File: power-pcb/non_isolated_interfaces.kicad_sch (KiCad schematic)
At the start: 66 parts, among them J1 Network Connector, J2 Screw_Terminal_01x02, J3 STDC14, J4 USB_C_Receptacle_USB2.0_16P, U1 TPS5430DDA, U2 ECMF02-2AMX6, U3 AMS1117-3.3, U4 SN65HVD230

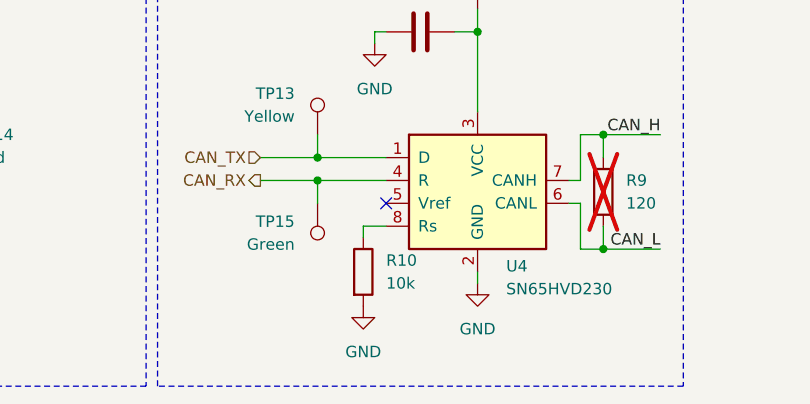
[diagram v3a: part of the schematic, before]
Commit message: power-pcb: change some 10k to 12k
JLCPCB doesn't offer a small package for the 10k resistors so some had
to be changed.
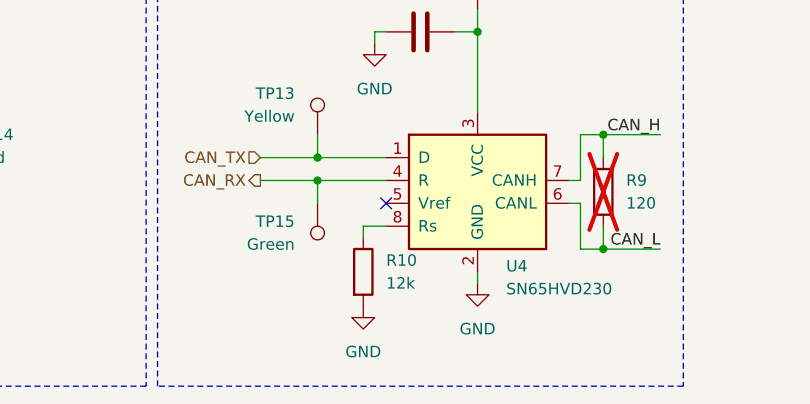
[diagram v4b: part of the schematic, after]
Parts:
- R1, R2: footprint Resistor_SMD:R_0603_1608Metric_Pad0.98x0.95mm_HandSolder -> Resistor_SMD:R_0805_2012Metric_Pad1.20x1.40mm_HandSolder; JLCPCB C25804 -> C17414
- R10: value 10k -> 12k; footprint Resistor_SMD:R_0603_1608Metric_Pad0.98x0.95mm_HandSolder -> Resistor_SMD:R_0402_1005Metric_Pad0.72x0.64mm_HandSolder; JLCPCB C25804 -> C25752
- R4: footprint Resistor_SMD:R_0402_1005Metric_Pad0.72x0.64mm_HandSolder -> Resistor_SMD:R_0603_1608Metric_Pad0.98x0.95mm_HandSolder; JLCPCB C11702 -> C21190
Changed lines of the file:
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@@
 	(title_block
 		(title "Non-Isolated Interfaces and Power")
-		(date "2026-06-13")
+		(date "2026-06-19")
 		(rev "v1.1.0")
 	)
@@
 			)
 		)
-		(property "Value" "10k"
+		(property "Value" "12k"
 			(at 142.24 185.4199 0)
 			(show_name no)
@@
 			)
 		)
-		(property "Footprint" "Resistor_SMD:R_0603_1608Metric_Pad0.98x0.95mm_HandSolder"
+		(property "Footprint" "Resistor_SMD:R_0402_1005Metric_Pad0.72x0.64mm_HandSolder"
 			(at 137.922 184.15 90)
 			(hide yes)
@@
 			)
 		)
-		(property "JLCPCB" "C25804"
+		(property "JLCPCB" "C25752"
 			(at 139.7 184.15 0)
 			(hide yes)
@@
 			)
 		)
-		(property "Footprint" "Resistor_SMD:R_0603_1608Metric_Pad0.98x0.95mm_HandSolder"
+		(property "Footprint" "Resistor_SMD:R_0805_2012Metric_Pad1.20x1.40mm_HandSolder"
 			(at 206.502 33.02 90)
 			(hide yes)
@@
 			)
 		)
-		(property "JLCPCB" "C25804"
+		(property "JLCPCB" "C17414"
 			(at 208.28 33.02 0)
 			(hide yes)
@@
 			)
 		)
-		(property "Footprint" "Resistor_SMD:R_0603_1608Metric_Pad0.98x0.95mm_HandSolder"
+		(property "Footprint" "Resistor_SMD:R_0805_2012Metric_Pad1.20x1.40mm_HandSolder"
 			(at 244.602 33.02 90)
 			(hide yes)
@@
 			)
 		)
-		(property "JLCPCB" "C25804"
+		(property "JLCPCB" "C17414"
 			(at 246.38 33.02 0)
 			(hide yes)
@@
 			)
 		)
-		(property "Footprint" "Resistor_SMD:R_0402_1005Metric_Pad0.72x0.64mm_HandSolder"
+		(property "Footprint" "Resistor_SMD:R_0603_1608Metric_Pad0.98x0.95mm_HandSolder"
 			(at 270.002 33.02 90)
 			(hide yes)
@@
 			)
 		)
-		(property "JLCPCB" "C11702"
+		(property "JLCPCB" "C21190"
 			(at 271.78 33.02 0)
 			(hide yes)

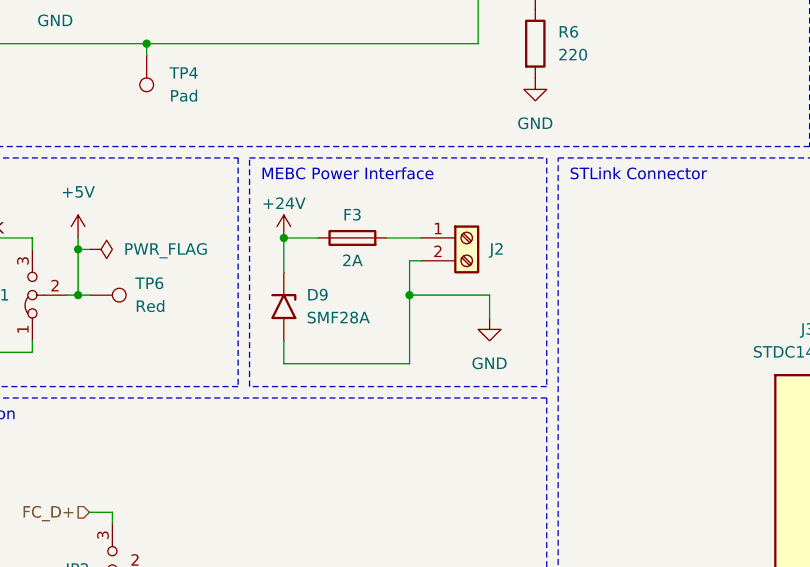
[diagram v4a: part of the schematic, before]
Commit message: power-pcb: finish placement and started routing
Started routing power traces only and didn't place test points yet.
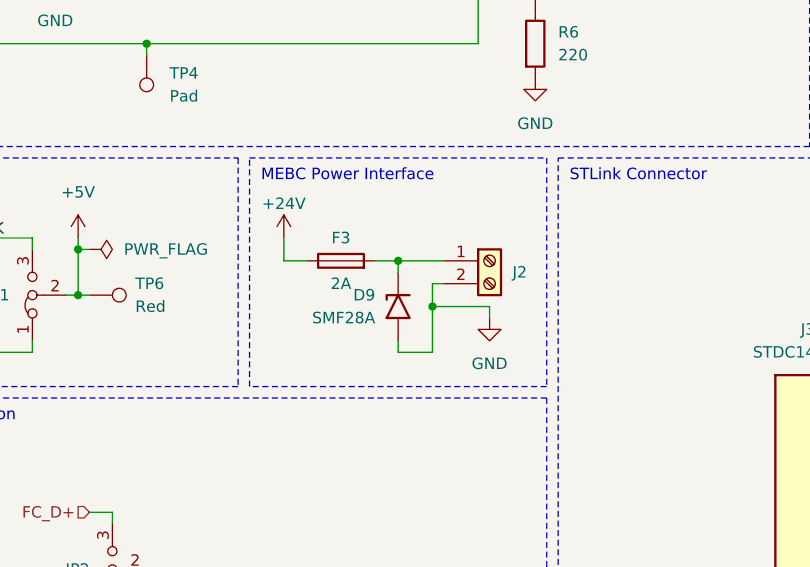
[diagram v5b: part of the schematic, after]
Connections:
- net +24V: no longer D9.1 (A1)
- net at F3.2, J2.1 (Pin_1): now also D9.1 (A1)
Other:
- moved on the sheet: D9, F3, J2
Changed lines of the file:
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@@
 	)
 	(junction
+		(at 193.04 74.93)
+		(diameter 0)
+		(color 0 0 0 0)
+	)
+	(junction
 		(at 166.37 168.91)
 		(diameter 0)
@@
 	)
 	(junction
+		(at 196.85 80.01)
+		(diameter 0)
+		(color 0 0 0 0)
+	)
+	(junction
 		(at 76.2 24.13)
 		(diameter 0)
@@
 	)
 	(junction
-		(at 180.34 72.39)
-		(diameter 0)
-		(color 0 0 0 0)
-	)
-	(junction
 		(at 85.09 170.18)
 		(diameter 0)
@@
 	)
 	(junction
-		(at 194.31 78.74)
-		(diameter 0)
-		(color 0 0 0 0)
-	)
-	(junction
 		(at 173.99 38.1)
 		(diameter 0)
@@
 	(wire
 		(pts
-			(xy 191.77 72.39) (xy 195.58 72.39)
+			(xy 190.5 74.93) (xy 193.04 74.93)
 		)
 		(stroke
@@
 	(wire
 		(pts
+			(xy 193.04 74.93) (xy 198.12 74.93)
+		)
+		(stroke
+			(width 0)
+			(type default)
+		)
+	)
+	(wire
+		(pts
 			(xy 30.48 130.81) (xy 30.48 129.54)
 		)
@@
 	(wire
 		(pts
+			(xy 193.04 74.93) (xy 193.04 76.2)
+		)
+		(stroke
+			(width 0)
+			(type default)
+		)
+	)
+	(wire
+		(pts
 			(xy 161.29 133.35) (xy 161.29 132.08)
 		)
@@
 	(wire
 		(pts
-			(xy 180.34 76.2) (xy 180.34 72.39)
-		)
-		(stroke
-			(width 0)
-			(type default)
-		)
-	)
-	(wire
-		(pts
 			(xy 41.91 31.75) (xy 41.91 43.18)
 		)
@@
 	(wire
 		(pts
-			(xy 194.31 78.74) (xy 194.31 86.36)
-		)
-		(stroke
-			(width 0)
-			(type default)
-		)
-	)
-	(wire
-		(pts
 			(xy 97.79 26.67) (xy 97.79 27.94)
 		)
@@
 	(wire
 		(pts
-			(xy 180.34 72.39) (xy 184.15 72.39)
-		)
-		(stroke
-			(width 0)
-			(type default)
-		)
-	)
-	(wire
-		(pts
 			(xy 97.79 36.83) (xy 97.79 38.1)
 		)
@@
 	(wire
 		(pts
+			(xy 196.85 80.01) (xy 196.85 85.09)
+		)
+		(stroke
+			(width 0)
+			(type default)
+		)
+	)
+	(wire
+		(pts
 			(xy 86.36 78.74) (xy 90.17 78.74)
 		)
@@
 	(wire
 		(pts
-			(xy 203.2 78.74) (xy 203.2 81.28)
+			(xy 203.2 80.01) (xy 203.2 81.28)
 		)
 		(stroke
@@
 	(wire
 		(pts
+			(xy 180.34 72.39) (xy 180.34 74.93)
+		)
+		(stroke
+			(width 0)
+			(type default)
+		)
+	)
+	(wire
+		(pts
 			(xy 49.53 135.89) (xy 49.53 137.16)
 		)
@@
 	(wire
 		(pts
+			(xy 193.04 85.09) (xy 196.85 85.09)
+		)
+		(stroke
+			(width 0)
+			(type default)
+		)
+	)
+	(wire
+		(pts
 			(xy 55.88 106.68) (xy 63.5 106.68)
 		)
@@
 	(wire
 		(pts
+			(xy 180.34 74.93) (xy 182.88 74.93)
+		)
+		(stroke
+			(width 0)
+			(type default)
+		)
+	)
+	(wire
+		(pts
 			(xy 173.99 39.37) (xy 173.99 38.1)
 		)
@@
 	(wire
 		(pts
+			(xy 193.04 83.82) (xy 193.04 85.09)
+		)
+		(stroke
+			(width 0)
+			(type default)
+		)
+	)
+	(wire
+		(pts
 			(xy 63.5 87.63) (xy 63.5 88.9)
 		)
@@
 	(wire
 		(pts
-			(xy 203.2 78.74) (xy 194.31 78.74)
+			(xy 203.2 80.01) (xy 196.85 80.01)
 		)
 		(stroke
@@
 	(wire
 		(pts
-			(xy 194.31 74.93) (xy 195.58 74.93)
+			(xy 196.85 77.47) (xy 198.12 77.47)
 		)
 		(stroke
@@
 	(wire
 		(pts
-			(xy 194.31 74.93) (xy 194.31 78.74)
+			(xy 196.85 77.47) (xy 196.85 80.01)
 		)
 		(stroke
@@
 	(wire
 		(pts
-			(xy 180.34 86.36) (xy 194.31 86.36)
-		)
-		(stroke
-			(width 0)
-			(type default)
-		)
-	)
-	(wire
-		(pts
 			(xy 45.72 91.44) (xy 46.99 91.44)
 		)
@@
 	(wire
 		(pts
-			(xy 180.34 83.82) (xy 180.34 86.36)
-		)
-		(stroke
-			(width 0)
-			(type default)
-		)
-	)
-	(wire
-		(pts
 			(xy 134.62 173.99) (xy 142.24 173.99)
 		)
@@
 	(symbol
 		(lib_id "Diode:SMF28A")
-		(at 180.34 80.01 270)
+		(at 193.04 80.01 90)
+		(mirror x)
 		(unit 1)
 		(body_style 1)
@@
 		(dnp no)
 		(property "Reference" "D9"
-			(at 182.88 78.7399 90)
+			(at 190.5 78.7399 90)
 			(show_name no)
 			(do_not_autoplace no)
@@
 		)
 		(property "Value" "SMF28A"
-			(at 182.88 81.2799 90)
+			(at 190.5 81.2799 90)
 			(show_name no)
 			(do_not_autoplace no)
@@
 		)
 		(property "Footprint" "Diode_SMD:D_SMF"
-			(at 175.26 80.01 0)
+			(at 198.12 80.01 0)
 			(hide yes)
 			(show_name no)
@@
 		)
 		(property "Datasheet" "https://www.vishay.com/doc?85881"
-			(at 180.34 78.74 0)
+			(at 193.04 78.74 0)
 			(hide yes)
 			(show_name no)
@@
 		)
 		(property "Description" "200W unidirectional Transil Transient Voltage Suppressor, 28Vrwm, SMF"
-			(at 180.34 80.01 0)
+			(at 193.04 80.01 0)
 			(hide yes)
 			(show_name no)
@@
 		)
 		(property "JLCPCB" "C41376091"
-			(at 180.34 80.01 90)
+			(at 193.04 80.01 90)
 			(hide yes)
 			(show_name no)
@@
 		)
 		(property "Sim.Library" ""
-			(at 180.34 80.01 90)
+			(at 193.04 80.01 90)
 			(hide yes)
 			(show_name no)
@@
 		)
 		(property "Sim.Name" ""
-			(at 180.34 80.01 90)
+			(at 193.04 80.01 90)
 			(hide yes)
 			(show_name no)
@@
 	(symbol
 		(lib_id "Device:Fuse")
-		(at 187.96 72.39 90)
+		(at 186.69 74.93 90)
 		(unit 1)
 		(body_style 1)
@@
 		(dnp no)
 		(property "Reference" "F3"
-			(at 187.96 69.85 90)
+			(at 186.69 72.39 90)
 			(show_name no)
 			(do_not_autoplace no)
@@
 		)
 		(property "Value" "2A"
-			(at 187.96 74.93 90)
+			(at 186.69 77.47 90)
 			(show_name no)
 			(do_not_autoplace no)
@@
 		)
 		(property "Footprint" "Exocet:Fuseholder_Littelfuse_Combined"
-			(at 187.96 74.168 90)
+			(at 186.69 76.708 90)
 			(hide yes)
 			(show_name no)
@@
 		)
 		(property "Datasheet" ""
-			(at 187.96 72.39 0)
+			(at 186.69 74.93 0)
 			(hide yes)
 			(show_name no)
@@
 		)
 		(property "Description" "Fuse"
-			(at 187.96 72.39 0)
+			(at 186.69 74.93 0)
 			(hide yes)
 			(show_name no)
@@
 		)
 		(property "MFR" "Littelfuse Inc."
-			(at 187.96 72.39 90)
+			(at 186.69 74.93 90)
 			(hide yes)
 			(show_name no)
@@
 		)
 		(property "MPN" "01110501Z"
-			(at 187.96 72.39 90)
+			(at 186.69 74.93 90)
 			(hide yes)
 			(show_name no)
@@
 	(symbol
 		(lib_id "Connector:Screw_Terminal_01x02")
-		(at 200.66 72.39 0)
+		(at 203.2 74.93 0)
 		(unit 1)
 		(body_style 1)
@@
 		(dnp no)
 		(property "Reference" "J2"
-			(at 203.2 73.66 0)
+			(at 205.74 76.2 0)
 			(show_name no)
 			(do_not_autoplace no)
@@
 		)
 		(property "Value" "Screw_Terminal_01x02"
-			(at 203.2 74.9299 0)
+			(at 205.74 77.4699 0)
 			(hide yes)
 			(show_name no)
@@
 		)
 		(property "Footprint" "Exocet:Wuerth_Term_Blk_2pos_Side_Entry_5mm"
-			(at 200.66 72.39 0)
+			(at 203.2 74.93 0)
 			(hide yes)
 			(show_name no)
@@
 		)
 		(property "Datasheet" ""
-			(at 200.66 72.39 0)
+			(at 203.2 74.93 0)
 			(hide yes)
 			(show_name no)
@@
 		)
 		(property "Description" "For MEBC Power Interface"
-			(at 210.82 68.58 0)
+			(at 213.36 71.12 0)
 			(hide yes)
 			(show_name no)
@@
 		)
 		(property "MFR" "Wuerth Eletronik"
-			(at 200.66 72.39 0)
+			(at 203.2 74.93 0)
 			(hide yes)
 			(show_name no)
@@
 		)
 		(property "MPN" "691137710002"
-			(at 200.66 72.39 0)
+			(at 203.2 74.93 0)
 			(hide yes)
 			(show_name no)
@@
 		)
 		(property "Sim.Library" ""
-			(at 200.66 72.39 0)
+			(at 203.2 74.93 0)
 			(hide yes)
 			(show_name no)
@@
 		)
 		(property "Sim.Name" ""
-			(at 200.66 72.39 0)
+			(at 203.2 74.93 0)
 			(hide yes)
 			(show_name no)
